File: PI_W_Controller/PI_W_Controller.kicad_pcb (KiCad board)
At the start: 2 copper layers, 84.8 x 88.1 mm, 41 parts, among them J1 String1, J10 Vin Select, J11 Raspberry_Pi_2_3, J12 User Input, J2 String2, J3 String3, J4 String4, J5 String5, J6 String6, J7 String7, J8 String8, J9 OLED, U1 SN74HCT245N, U2 LM7805

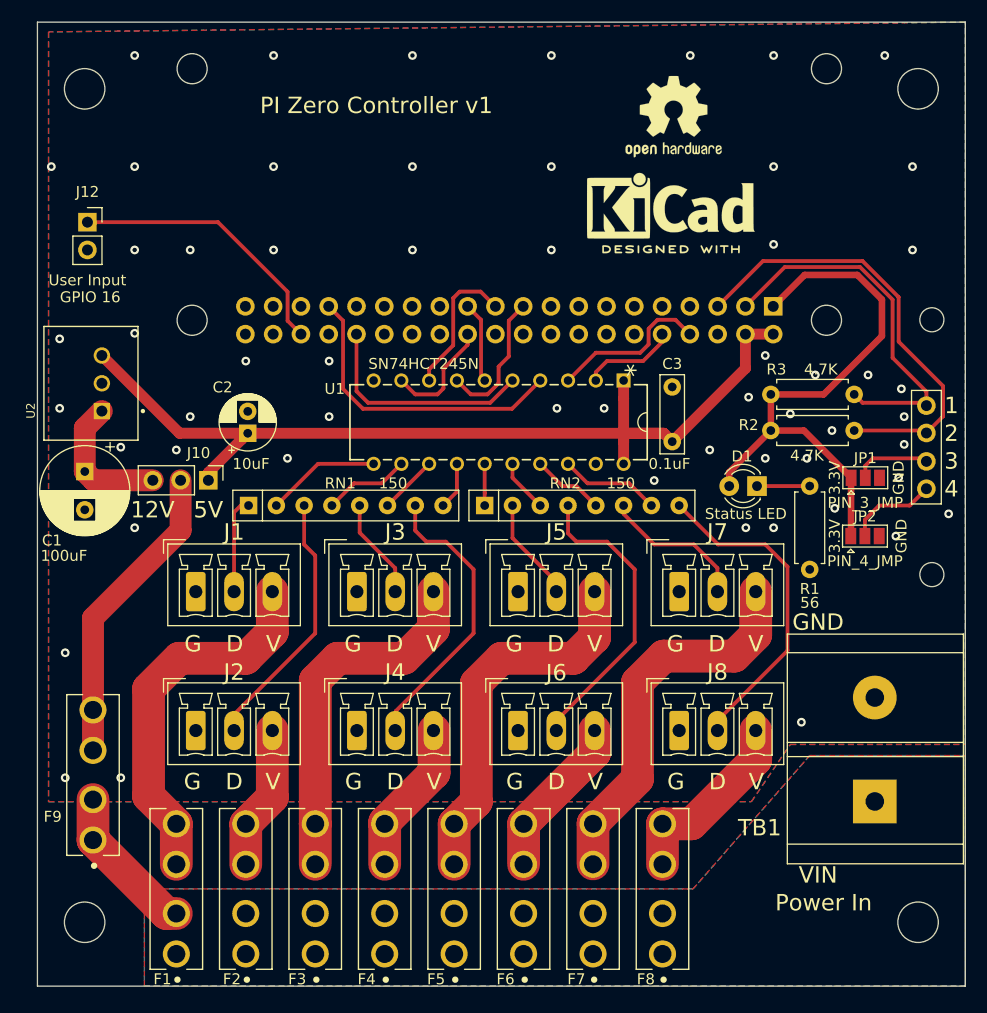
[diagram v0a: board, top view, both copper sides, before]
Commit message: changed pinout to match FPP and added Expansion port
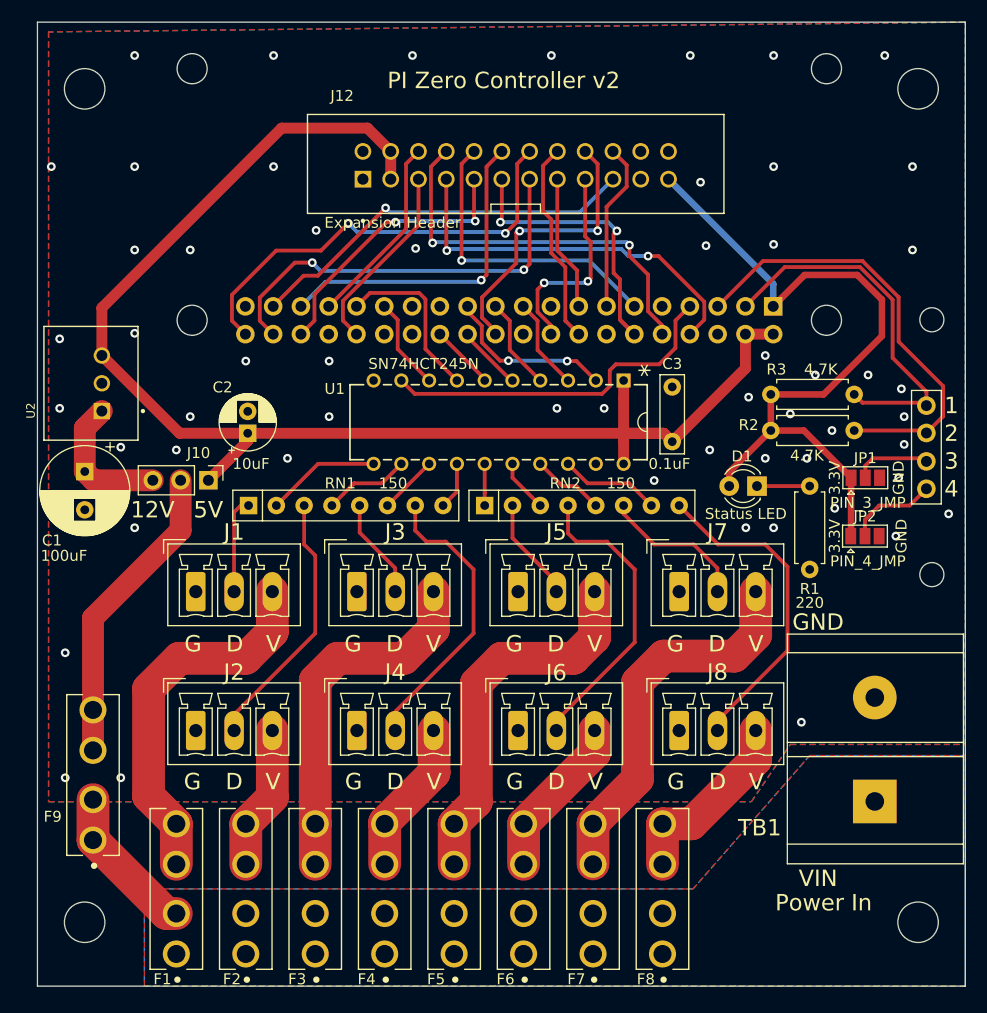
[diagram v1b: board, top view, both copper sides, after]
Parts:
- removed REF**: OSHW-Logo2_9.8x8mm_SilkScreen, Symbol:OSHW-Logo2_9.8x8mm_SilkScreen
- removed REF**: KiCad-Logo2_6mm_SilkScreen, Symbol:KiCad-Logo2_6mm_SilkScreen
- J12: value User Input -> Expansion Header; footprint Connector_PinSocket_2.54mm:PinSocket_1x02_P2.54mm_Vertical -> 302-S241:OST_302-S241
- R1: value 56 -> 220
- moved J12 39.5 mm to (159.3, 58.3)
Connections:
- J11 pad 10: Data8 -> OUT12
- J11 pad 11: unconnected-(J11-Pad11) -> OUT14
- J11 pad 12: unconnected-(J11-Pad12) -> OUT15
- J11 pad 13: unconnected-(J11-Pad13) -> OUT24
- J11 pad 15: unconnected-(J11-Pad15) -> OUT19
- J11 pad 16: unconnected-(J11-Pad16) -> OUT20
- J11 pad 18: unconnected-(J11-Pad18) -> OUT21
- J11 pad 19: Data3 -> Data7
- J11 pad 21: Data2 -> Data6
- J11 pad 22: unconnected-(J11-Pad22) -> OUT22
- J11 pad 23: Data4 -> Data8
- J11 pad 24: Data1 -> Data5
- J11 pad 26: unconnected-(J11-Pad26) -> Data4
- J11 pad 29: unconnected-(J11-Pad29) -> Data2
- J11 pad 31: unconnected-(J11-Pad31) -> Data3
- J11 pad 32: Data5 -> OUT9
- J11 pad 33: Data6 -> OUT10
- J11 pad 35: unconnected-(J11-Pad35) -> OUT16
- J11 pad 36: Net-(J11-Pad36) -> OUT13
- J11 pad 37: unconnected-(J11-Pad37) -> OUT23
- J11 pad 38: unconnected-(J11-Pad38) -> OUT17
- J11 pad 40: unconnected-(J11-Pad40) -> OUT18
- J11 pad 7: unconnected-(J11-Pad7) -> Data1
- J11 pad 8: Data7 -> OUT11
- J12 pad 1: Net-(J11-Pad36) -> GND
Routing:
- net +5V: track 88.6 -> 129.4 mm
- net OUT18: track 0.00 -> 40.6 mm, vias 0 -> 2
- net OUT17: track 0.00 -> 38.2 mm, vias 0 -> 2
- net OUT12: track 0.00 -> 36.5 mm, vias 0 -> 2
- net OUT23: track 0.00 -> 36.2 mm, vias 0 -> 1
- net OUT11: track 0.00 -> 35.7 mm, vias 0 -> 2
- net OUT16: track 0.00 -> 30.0 mm, vias 0 -> 1
- net OUT14: track 0.00 -> 28.0 mm, vias 0 -> 1
- net OUT15: track 0.00 -> 27.0 mm, vias 0 -> 2
- net OUT22: track 0.00 -> 26.4 mm, vias 0 -> 2
- net OUT13: track 0.00 -> 25.5 mm, vias 0 -> 2
- net Net-(J11-Pad36): track 25.3 -> 0.00 mm
- net Data1: track 10.5 -> 32.5 mm
- net Data6: track 27.9 -> 8.48 mm
- net OUT21: track 0.00 -> 19.1 mm, vias 0 -> 2
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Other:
- board text removed: "GPIO 16"
